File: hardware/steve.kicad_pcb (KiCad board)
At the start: 4 copper layers, 50 x 50 mm, 82 parts, among them J1 JST GH 6P Vertical 1A C189892, J2 JST GH 6P Vertical 1A C189892, J3 JST GH 6P Vertical 1A C189892, Q1 NMOS GSD 350mA 60V C282405, Q2 NMOS GSD 350mA 60V C282405, Q3 NMOS GSD 350mA 60V C282405, Q4 NMOS GSD 350mA 60V C282405, Q5 NMOS GSD 350mA 60V C282405, Q6 NMOS GSD 350mA 60V C282405

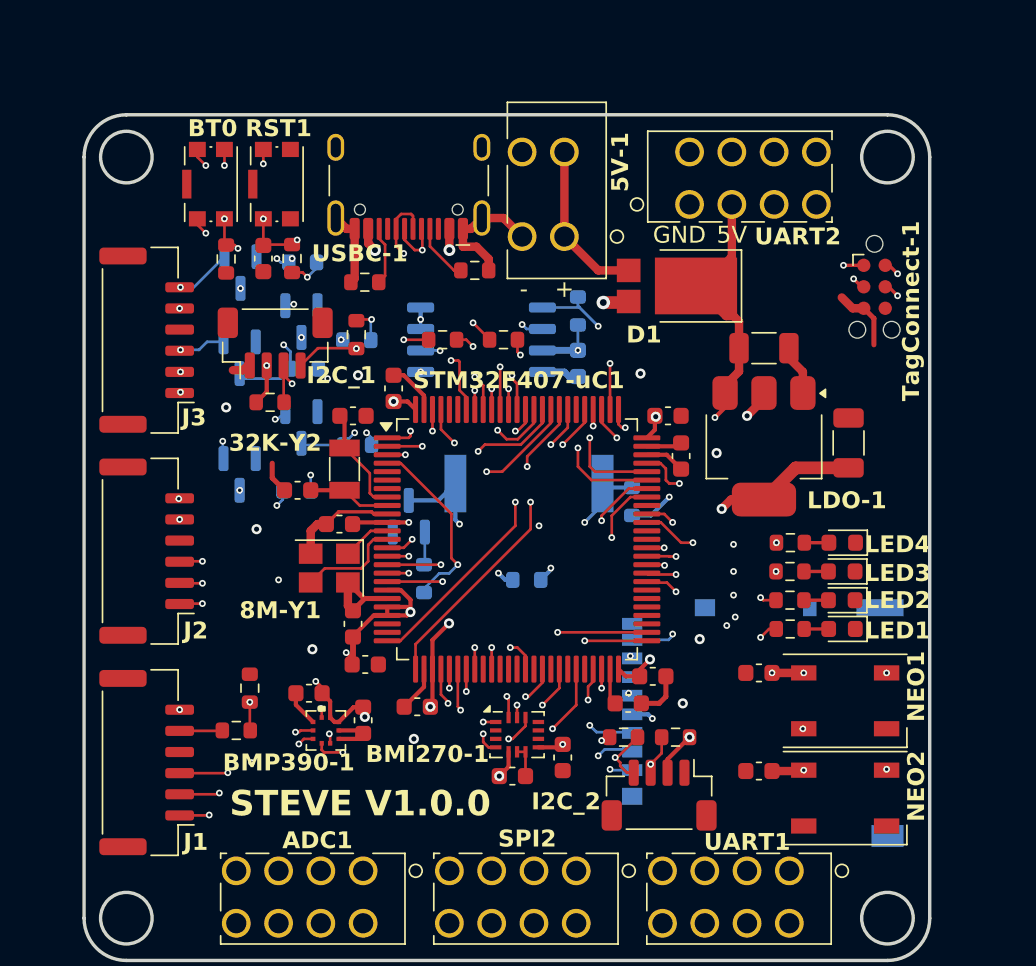
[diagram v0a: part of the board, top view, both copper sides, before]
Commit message: Fixed all ERC issues; fixed important DRC issues
Fixed all ERC Errors and Warnings in the schematic. Fixed all Errors and Warnings in the DRC for the board (Not counting JLC 4-Wire Kelvin test and plane thermal relief spoke errors that were manually reviewed and excluded).
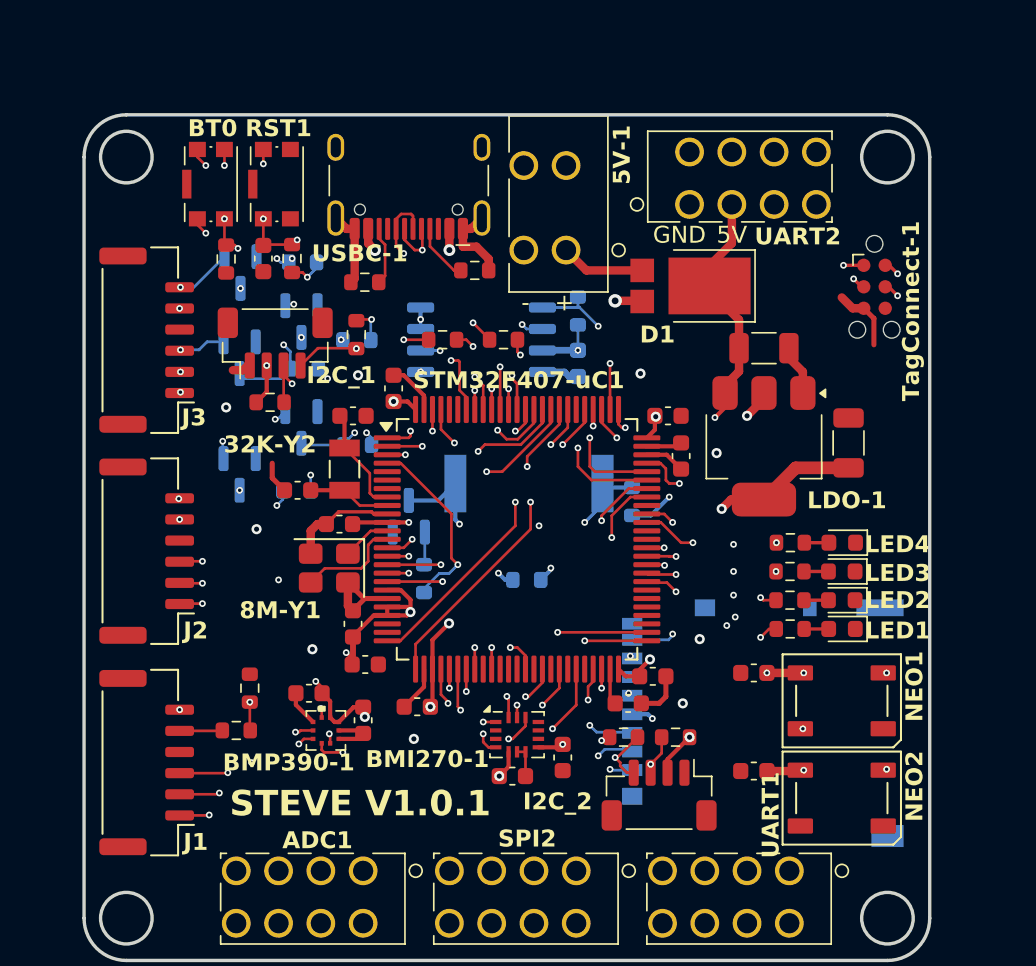
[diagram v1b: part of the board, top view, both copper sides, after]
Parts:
- 32K-Y2: footprint Crystal:Crystal_SMD_3215-2Pin_3.2x1.5mm -> Imported_Footprints:Crystal_SMD_3215-2Pin_3.2x1.5mm_Fixed
- moved 5V-1 0.81 mm to (127.6, 103.0)
- moved D1 0.80 mm to (135.9, 110.1)
- moved C32 0.30 mm to (139.6, 133.0)
- moved C33 0.30 mm to (139.6, 138.8)
- moved NEO1 0.20 mm to (144.8, 134.7)
- moved NEO2 0.20 mm to (144.8, 140.4)
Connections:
- USBC-1 pad A8: unconnected-(USBC-1-SBU1-PadA8) -> (no net)
- USBC-1 pad B8: unconnected-(USBC-1-SBU2-PadB8) -> (no net)
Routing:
- net GND: track 54.5 -> 51.7 mm
- net +5V: track 51.4 -> 50.6 mm
- net +5V_USB: track 22.0 -> 22.7 mm
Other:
- board text added: "STEVE V1.0.1"
- board text removed: "STEVE V1.0.0"

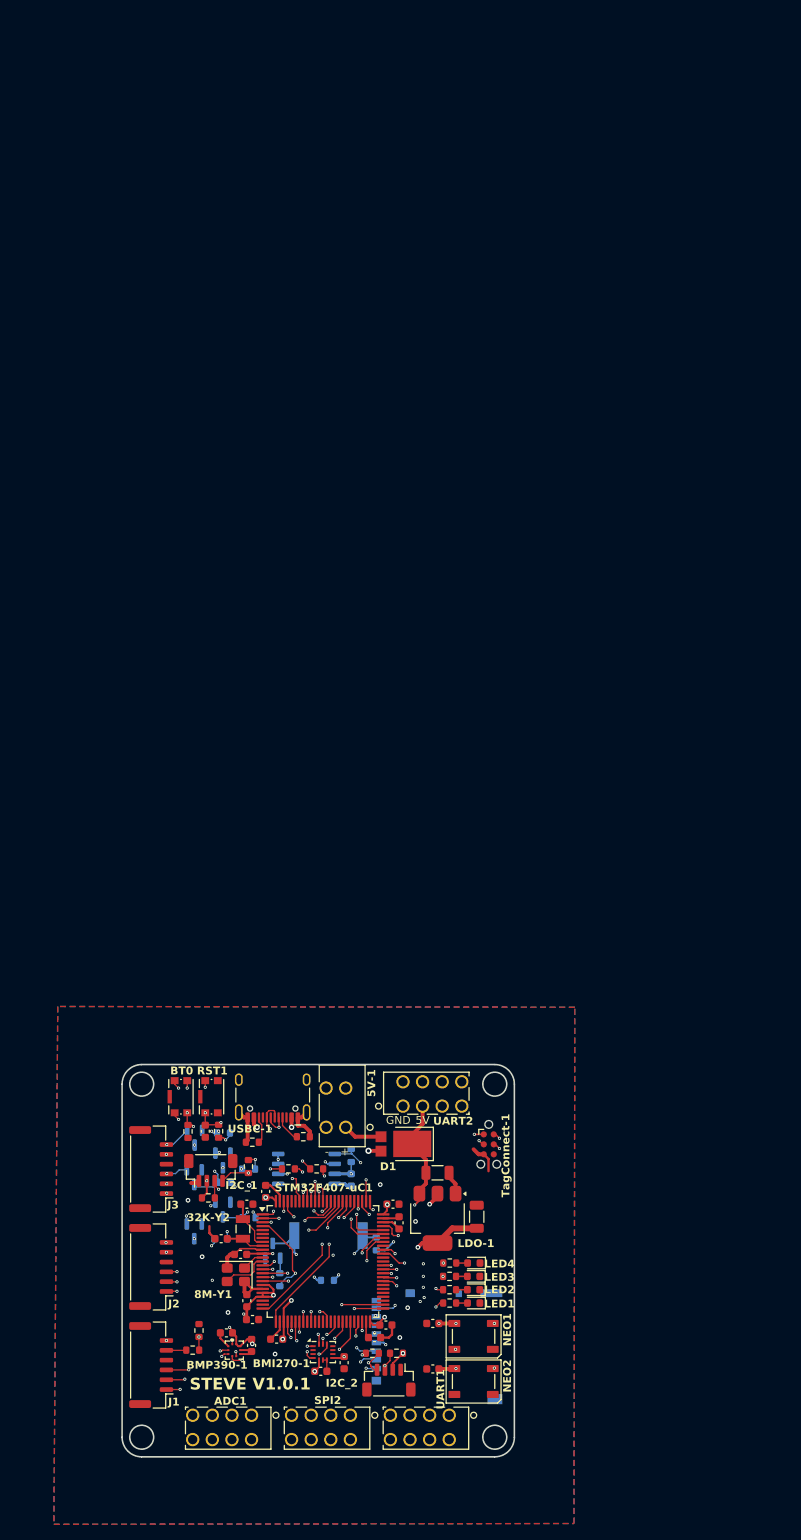
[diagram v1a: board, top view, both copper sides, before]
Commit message: Update board to 6 layers and single sided assembly
Update board to 6 layers and single sided assembly (all components placed on the same side); all footprints given an initial placement
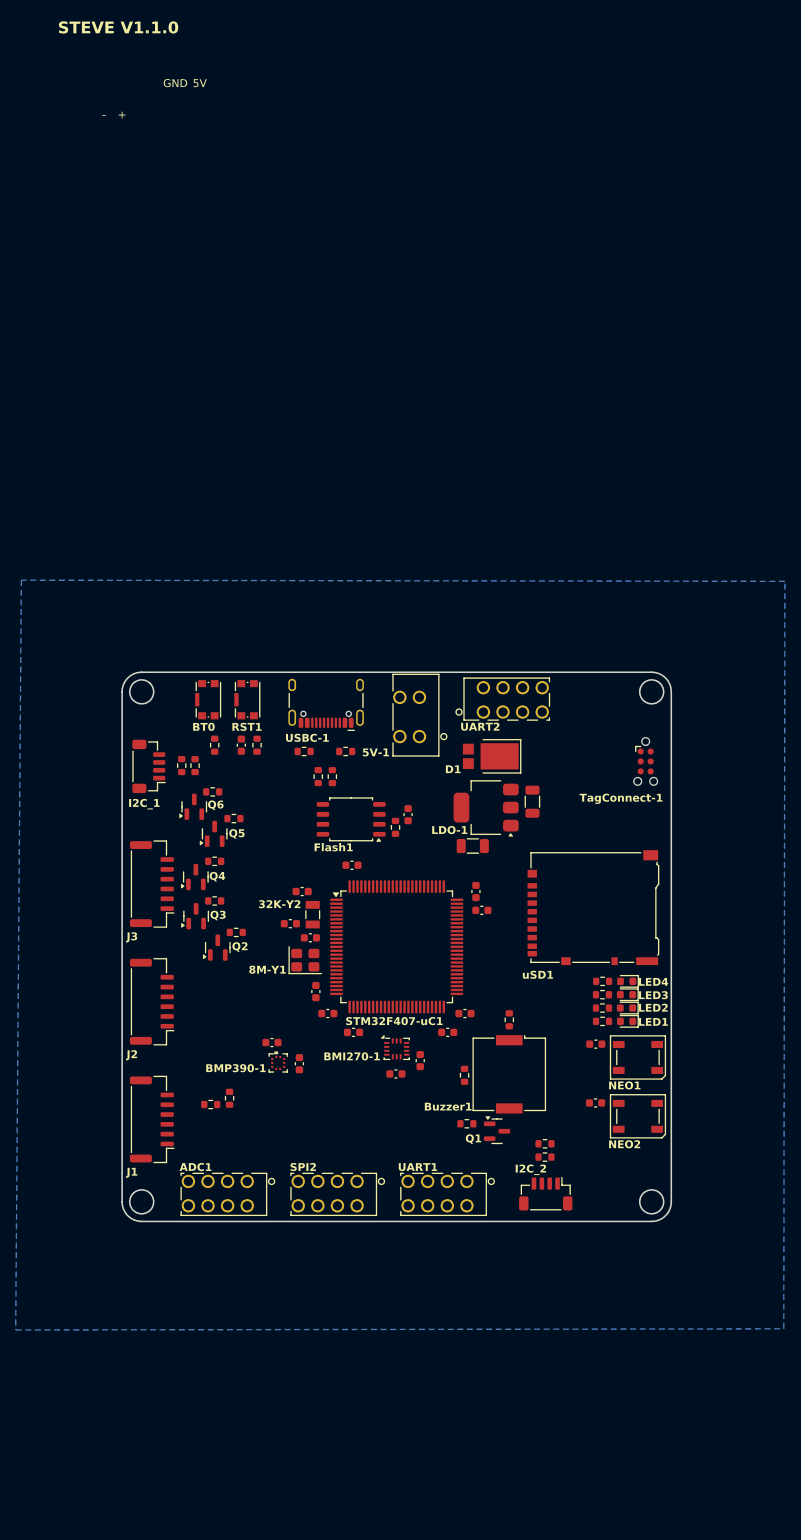
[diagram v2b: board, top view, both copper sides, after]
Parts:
- Buzzer1, C31, Flash1, Q1, Q2, Q3, Q4, Q5, Q6, R15, R20, R21, R22, R3, R4, R5, R6, R7, uSD1: moved to F.Cu
- moved uSD1 59.4 mm to (160.0, 80.0), turned to 90 degrees
- moved R17 55.2 mm to (107.6, 61.9), turned to -90 degrees
- moved TagConnect-1 52.7 mm to (166.7, 61.4)
- moved LDO-1 52.7 mm to (146.4, 67.2), turned to 180 degrees
- moved I2C_1 52.1 mm to (103.4, 62.0), turned to 90 degrees
- moved R16 51.6 mm to (109.3, 61.9), turned to -90 degrees
- moved UART2 51.3 mm to (152.0, 52.0)
- moved RST1 50.8 mm to (116.0, 53.5)
- moved USBC-1 50.8 mm to (126.0, 52.7)
- moved BT0 50.7 mm to (111.0, 53.5)
- moved 5V-1 50.7 mm to (137.0, 53.2)
- moved D1 50.6 mm to (147.0, 60.7)
- moved R13 50.2 mm to (123.2, 60.1)
- moved R12 50.1 mm to (125.0, 63.3), turned to -90 degrees
- moved R11 50.0 mm to (126.8, 63.3), turned to -90 degrees
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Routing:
- net +3.3V: track 261.1 -> 0.00 mm, vias 28 -> 0
- net ~{RESET}: track 67.2 -> 0.00 mm, vias 5 -> 0
- net GND: track 51.7 -> 0.00 mm, vias 9 -> 0
- net +5V: track 50.6 -> 0.00 mm, vias 5 -> 0
- net PC3_SPI2_MOSI: track 43.0 -> 0.00 mm, vias 2 -> 0
- net PC2_SPI2_MISO: track 42.9 -> 0.00 mm, vias 2 -> 0
- net UART2_TX: track 42.8 -> 0.00 mm, vias 1 -> 0
- net UART2_RX: track 42.8 -> 0.00 mm, vias 1 -> 0
- net PB13_SPI2_SCK: track 42.5 -> 0.00 mm, vias 2 -> 0
- net ADC_C1: track 35.5 -> 0.00 mm, vias 1 -> 0
- net SERVO_PWM_4: track 31.2 -> 0.00 mm, vias 3 -> 0
- net ADC_C0: track 30.3 -> 0.00 mm, vias 1 -> 0
- net UART1_RX_PWM_A10: track 29.1 -> 0.00 mm, vias 1 -> 0
- net UART1_TX_PWM_A9: track 29.1 -> 0.00 mm, vias 1 -> 0
- net CONT1: track 28.8 -> 0.00 mm, vias 4 -> 0
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- added copper zone on In1.Cu, net GND
- added copper zone on In3.Cu, net GND
- removed copper zone on F.Cu, net GND
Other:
- board size 50 x 50 mm -> 70 x 70 mm
- copper layers 4 -> 6
- board text added: "STEVE V1.1.0"
- board text removed: "STEVE V1.0.1"

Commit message: Routed 6 layer board; DRC passes
Finished routing the 6 layer board; All DRC issues resolved
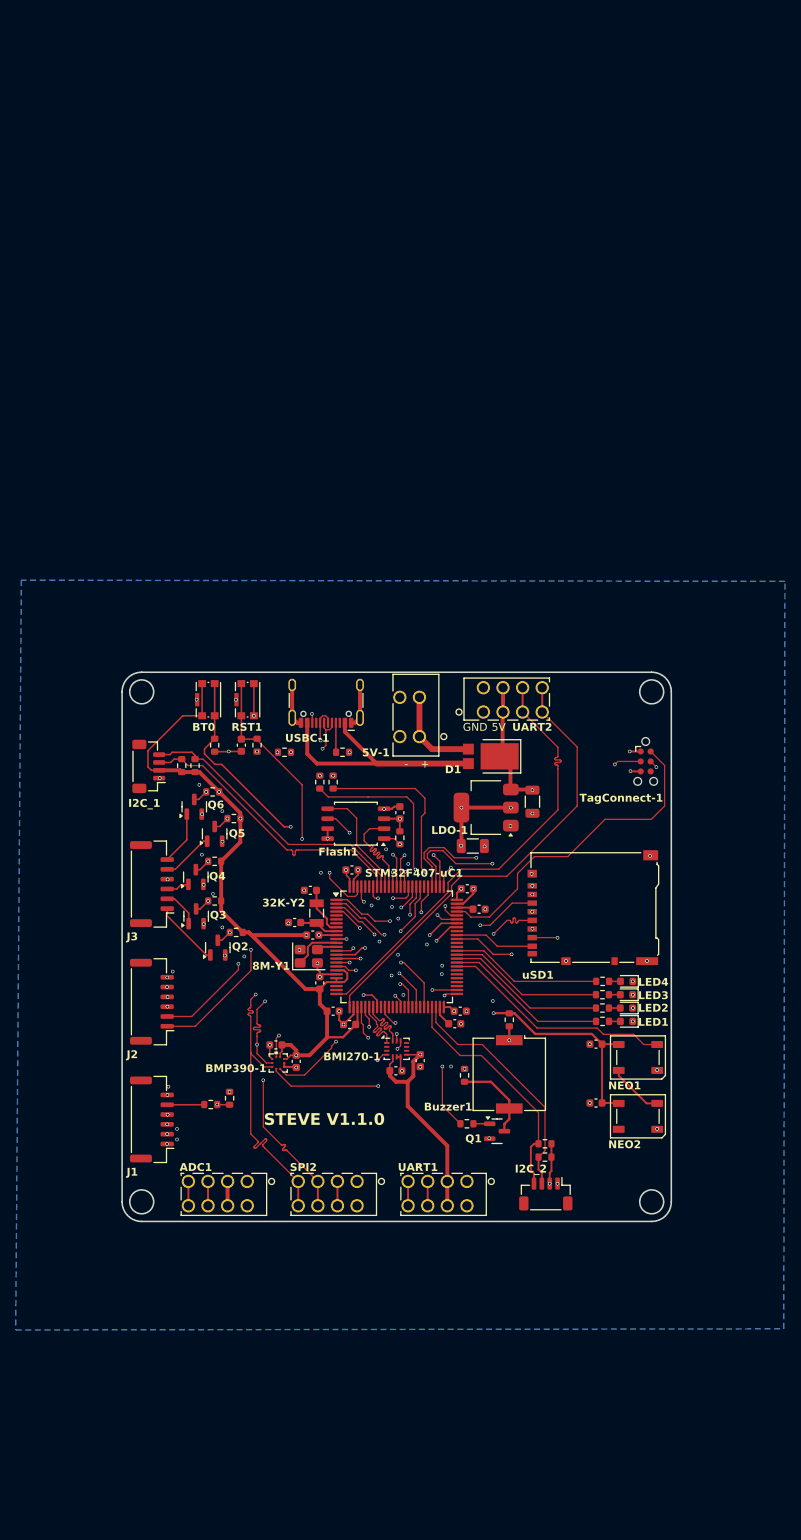
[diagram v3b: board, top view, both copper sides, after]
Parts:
- moved R13 2.50 mm to (120.7, 60.2)
- moved R12 2.02 mm to (126.9, 64.0)
- moved R11 1.75 mm to (125.2, 64.0)
- moved R15 1.43 mm to (135.4, 71.1)
- moved C1 1.42 mm to (142.4, 94.8)
- moved C9 1.21 mm to (125.2, 89.6)
- moved C12 1.15 mm to (144.0, 77.6), turned to 0 degrees
- moved C10 1.12 mm to (129.0, 94.9)
- moved C31 1.08 mm to (135.4, 67.9)
- moved C5 1.06 mm to (124.0, 77.8)
- moved Flash1 0.81 mm to (129.8, 69.3)
- moved C14 0.74 mm to (126.9, 93.2)
- moved 8M-Y1 0.67 mm to (123.8, 86.2)
- moved C11 0.67 mm to (143.1, 93.2)
- moved C13 0.60 mm to (129.3, 75.2)
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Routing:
- net +3.3V: track 0.00 -> 299.6 mm, vias 0 -> 18
- net ~{RESET}: track 0.00 -> 90.6 mm, vias 0 -> 3
- net +5V: track 0.00 -> 75.7 mm, vias 0 -> 2
- net UART2_TX: track 0.00 -> 58.0 mm
- net UART2_RX: track 0.00 -> 58.0 mm
- net PB13_SPI2_SCK: track 0.00 -> 53.4 mm, vias 0 -> 2
- net PC2_SPI2_MISO: track 0.00 -> 53.4 mm, vias 0 -> 2
- net PC3_SPI2_MOSI: track 0.00 -> 52.7 mm, vias 0 -> 4
- net ADC_C0: track 0.00 -> 52.5 mm, vias 0 -> 1
- net ADC_C1: track 0.00 -> 52.0 mm, vias 0 -> 1
- net GND: track 0.00 -> 48.0 mm, vias 0 -> 78
- net SERVO_PWM_4: track 0.00 -> 44.6 mm, vias 0 -> 2
- net MOSFET_3: track 0.00 -> 44.1 mm, vias 0 -> 2
- net Buzzer: track 0.00 -> 43.4 mm, vias 0 -> 3
- net SERVO_PWM_3: track 0.00 -> 43.0 mm, vias 0 -> 2
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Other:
- board text added: "{dblquote}He had such a knowledge of the dark side that he could even keep the ones he cared about from dying. The dark side of the Force is a pathway to many abilities some consider to be unnatural. He became so powerful… the only thing he was afraid of was losing his power, which eventually, of course, he did. Unfortunately, he taught his apprentice everything he knew, then his apprentice kille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"

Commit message: Created STEVE footprint; added image to PCB
Created STEVE image footprint with KiCad bitmap image tool; added footprint to imported footprints library; manually added new footprint to PCB.
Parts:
- added G***: LOGO, Imported_Footprints:STEVE-3D-Image, B.Cu at (146.8, 81.8)
